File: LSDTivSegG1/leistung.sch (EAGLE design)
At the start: 0 parts

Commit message: developed hard
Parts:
- added C1, C6: 10u, rcl:CPOL-EUE2.5-5
- added C10, C4, C5, C9: 100n, rcl:C-EU025-025X050
- added C2, C3, C7, C8: 1u, rcl:CPOL-EUE2.5-5
- added D1, D2, D7, D8: 1N4001, diode:1N4004
- added D10, D11, D12, D3, D4, D5, D6, D9: 18, diode:ZENER-DIODEZD-10
- added F1, F2, F3: (no value), special:FUSE
- added IC1, IC2, IC3, IC6: IR2184D, irs:IR2184D
- added IC4: 4081N, 40xx:4081N
- added IC5: 4069N, 40xx:4069N
- added Q1, Q2, Q3, Q4, Q5, Q6, Q7, Q8: (no value), transistor-power:PMOSFET_NTO220BV
- added R1, R10, R11, R12, R2, R3, R4, R9: 10, rcl:R-EU_0207/7
- added R13, R14, R15, R16, R5, R6, R7, R8: 47k, rcl:R-EU_0207/7
- added U$1: POWER, lsd2016:POWER
- added X1: 057-010-1, con-panduit:057-010-1
- added X2: MKDSN1,5/2-5,08, con-phoenix-508:MKDSN1,5/2-5,08
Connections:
- new net +15V: C10.1, C4.1, C5.1, C9.1, D1.A, D2.A, D7.A, D8.A, IC1.VCC, IC2.VCC, IC3.VCC, IC6.VCC
- new net +24V: F1.2
- new net +24_HORN: F2.2, F3.2, X2-2.KL
- new net 5V_OUT: X1-1.S
- new net BAT_+: C1.+, C6.+, F1.1, F2.1, F3.1, Q1.D, Q2.D, Q5.D, Q7.D, U$1.BAT_24V_+
- new net BAT_-: C1.-, C10.2, C4.2, C5.2, C6.-, C9.2, IC1.COM, IC2.COM, IC3.COM, IC6.COM, Q3.S, Q4.S, Q6.S, Q8.S, U$1.BAT_24V_-, X2-1.KL
- new net BAT_PWM_OUT: X1-6.S
- new net DIRL_IN: IC1.IN, IC2.IN, IC5A.I, X1-5.S
- new net DIRL_INV: IC3.IN, IC6.IN
- new net DIRL_IN_INV: IC5A.O
- new net DIRR_IN: IC5B.I, X1-7.S
- new net DIRR_IN_INV: IC5B.O
- new net ENABLE: IC4A.I0, IC4B.I0, X1-9.S
- new net GND_OUT: X1-3.S
- new net MOTOR_L_+: C2.-, C7.-, D10.A, D3.A, D4.A, D9.A, IC1.VS, IC2.VS, Q1.S, Q3.D, Q5.S, Q6.D, R15.2, R16.1, R7.2, R8.1, U$1.MOTOR_L_+
- new net MOTOR_L_-: C3.-, C8.-, D11.A, D12.A, D5.A, D6.A, IC3.VS, IC6.VS, Q2.S, Q4.D, Q7.S, Q8.D, R13.1, R14.2, R5.1, R6.2, U$1.MOTOR_L_-
- new net MOTOR_L_ACTIVE: IC1.!SD, IC2.!SD, IC3.!SD, IC4A.O, IC6.!SD
- new net MOTOR_PWM_L: IC4A.I1, X1-2.S
- new net MOTOR_PWM_R: IC4B.I1, X1-4.S
- new net MOTOR_R_+: U$1.MOTOR_R_+
- new net MOTOR_R_-: U$1.MOTOR_R_-
- new net MOTOR_R_ACTIVE: IC4B.O
- new net N$1: IC4P.VDD
- new net N$10: IC2.HO, R1.1
- new net N$11: IC3.HO, R4.2
- new net N$12: IC3.LO, R3.2
- new net N$13: D10.C, Q6.G, R10.2, R15.1
- new net N$14: D9.C, Q5.G, R16.2, R9.2
- new net N$15: IC4C.O
- new net N$16: IC4D.O
- new net N$17: D12.C, Q7.G, R12.1, R13.2
- new net N$18: D11.C, Q8.G, R11.1, R14.1
- new net N$19: IC5C.O
- new net N$2: IC4P.VSS
- new net N$20: IC5C.I
- new net N$21: IC4C.I0
- new net N$22: IC4C.I1
- new net N$23: IC4D.I0
- new net N$24: IC4D.I1
- new net N$25: IC1.LO, R10.1
- new net N$26: IC1.HO, R9.1
- new net N$27: IC6.HO, R12.2
- new net N$28: IC6.LO, R11.2
- new net N$3: IC5P.VDD
- new net N$4: IC5P.VSS
- new net N$5: D4.C, Q3.G, R2.2, R7.1
- new net N$6: D3.C, Q1.G, R1.2, R8.2
- new net N$7: D6.C, Q2.G, R4.1, R5.2
- new net N$8: D5.C, Q4.G, R3.1, R6.1
- new net N$9: IC2.LO, R2.1
- new net NC: X1-8.S
- new net NC2: X1-10.S
- new net VB: C2.+, C3.+, C7.+, C8.+, D1.C, D2.C, D7.C, D8.C, IC1.VB, IC2.VB, IC3.VB, IC6.VB
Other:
- note added: "Control Logic Enable-Signal"
- note added: "Fuses"
- note added: "H-Bridge-1"
- note added: "Mosfets IRFB3077"
- note added: "Mosfets haben Freilaufdiode integriert 210A"
- note added: "Power-Connector"
- note added: "Regelungsboard-Connector"

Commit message: changed naming high/low voltage area
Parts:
- removed C10, C9: 100n, rcl:C-EU025-025X050
- removed C6: 10u, rcl:CPOL-EUE2.5-5
- removed C7, C8: 1u, rcl:CPOL-EUE2.5-5
- removed D10, D11, D12, D9: 18, diode:ZENER-DIODEZD-10
- removed D7, D8: 1N4001, diode:1N4004
- removed IC1, IC6: IR2184D, irs:IR2184D
- removed Q5, Q6, Q7, Q8: (no value), transistor-power:PMOSFET_NTO220BV
- removed R10, R11, R12, R9: 10, rcl:R-EU_0207/7
- removed R13, R14, R15, R16: 47k, rcl:R-EU_0207/7
- added C11: 10u, rcl:CPOL-EUE2.5-5
- added C12, C13: 1u, rcl:CPOL-EUE2.5-5
- added C14, C15: 100n, rcl:C-EU025-025X050
- added D13, D14: 1N4001, diode:1N4004
- added D15, D16, D17, D18: 18, diode:ZENER-DIODEZD-10
- added DC1: TMR, traco_tmr:TMR
- added IC7, IC8: IR2184D, irs:IR2184D
- added Q10, Q11, Q12, Q9: (no value), transistor-power:PMOSFET_NTO220BV
- added R17, R18, R19, R20: 10, rcl:R-EU_0207/7
- added R21, R22, R23, R24: 47k, rcl:R-EU_0207/7
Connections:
- net BAT_PWM_OUT renamed BAT_PWM_OUT_CTL
- removed net 5V_OUT: X1-1.S
- removed net GND_OUT: X1-3.S
- removed net N$13: D10.C, Q6.G, R10.2, R15.1
- removed net N$14: D9.C, Q5.G, R16.2, R9.2
- removed net N$17: D12.C, Q7.G, R12.1, R13.2
- removed net N$18: D11.C, Q8.G, R11.1, R14.1
- removed net N$25: IC1.LO, R10.1
- removed net N$26: IC1.HO, R9.1
- removed net N$27: IC6.HO, R12.2
- removed net N$28: IC6.LO, R11.2
- new net 5V_OUT_CTL: DC1.+VOUT, X1-1.S
- new net DIRL_IN_CTL: X1-5.S
- new net DIRR_INV: IC8.IN
- new net DIRR_IN_CTL: X1-7.S
- new net ENABLE_CTL: X1-9.S
- new net GND_OUT_CTL: DC1.-VOUT, X1-3.S
- new net MOTOR_PWM_L_CTL: X1-2.S
- new net MOTOR_PWM_R_CTL: X1-4.S
- new net N$29: D16.C, Q10.G, R18.2, R23.1
- new net N$30: D15.C, Q9.G, R17.2, R24.2
- new net N$31: D18.C, Q11.G, R20.1, R21.2
- new net N$32: D17.C, Q12.G, R19.1, R22.1
- new net N$33: IC7.LO, R18.1
- new net N$34: IC7.HO, R17.1
- new net N$35: IC8.HO, R20.2
- new net N$36: IC8.LO, R19.2
- net +15V: now also C14.1, C15.1, D13.A, D14.A, IC7.VCC, IC8.VCC; no longer C10.1, C9.1, D7.A, D8.A, IC1.VCC, IC6.VCC
- net +24V: now also DC1.+VIN
- net BAT_+: now also C11.+, Q11.D, Q9.D; no longer C6.+, Q5.D, Q7.D
- net BAT_-: now also C11.-, C14.2, C15.2, DC1.-VIN, IC7.COM, IC8.COM, Q10.S, Q12.S; no longer C10.2, C6.-, C9.2, IC1.COM, IC6.COM, Q6.S, Q8.S
- net DIRL_IN: no longer IC1.IN, X1-5.S
- net DIRL_INV: no longer IC6.IN
- net DIRR_IN: now also IC7.IN; no longer X1-7.S
- net ENABLE: no longer X1-9.S
- net MOTOR_L_+: no longer C7.-, D10.A, D9.A, IC1.VS, Q5.S, Q6.D, R15.2, R16.1
- net MOTOR_L_-: no longer C8.-, D11.A, D12.A, IC6.VS, Q7.S, Q8.D, R13.1, R14.2
- net MOTOR_L_ACTIVE: no longer IC1.!SD, IC6.!SD
- net MOTOR_PWM_L: no longer X1-2.S
- net MOTOR_PWM_R: no longer X1-4.S
- net MOTOR_R_+: now also C12.-, D15.A, D16.A, IC7.VS, Q10.D, Q9.S, R23.2, R24.1
- net MOTOR_R_-: now also C13.-, D17.A, D18.A, IC8.VS, Q11.S, Q12.D, R21.1, R22.2
- net MOTOR_R_ACTIVE: now also IC7.!SD, IC8.!SD
- net VB: now also C12.+, C13.+, D13.C, D14.C, IC7.VB, IC8.VB; no longer C7.+, C8.+, D7.C, D8.C, IC1.VB, IC6.VB
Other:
- note added: "DCDC Converter"
- note added: "H-Bridge-1-Left"
- note added: "H-Bridge-2-Right"
- note added: "On/Off NC for On State"
- note added: "_CTL indicates position on LOW-Voltage Side of board"
- note removed: "H-Bridge-1"

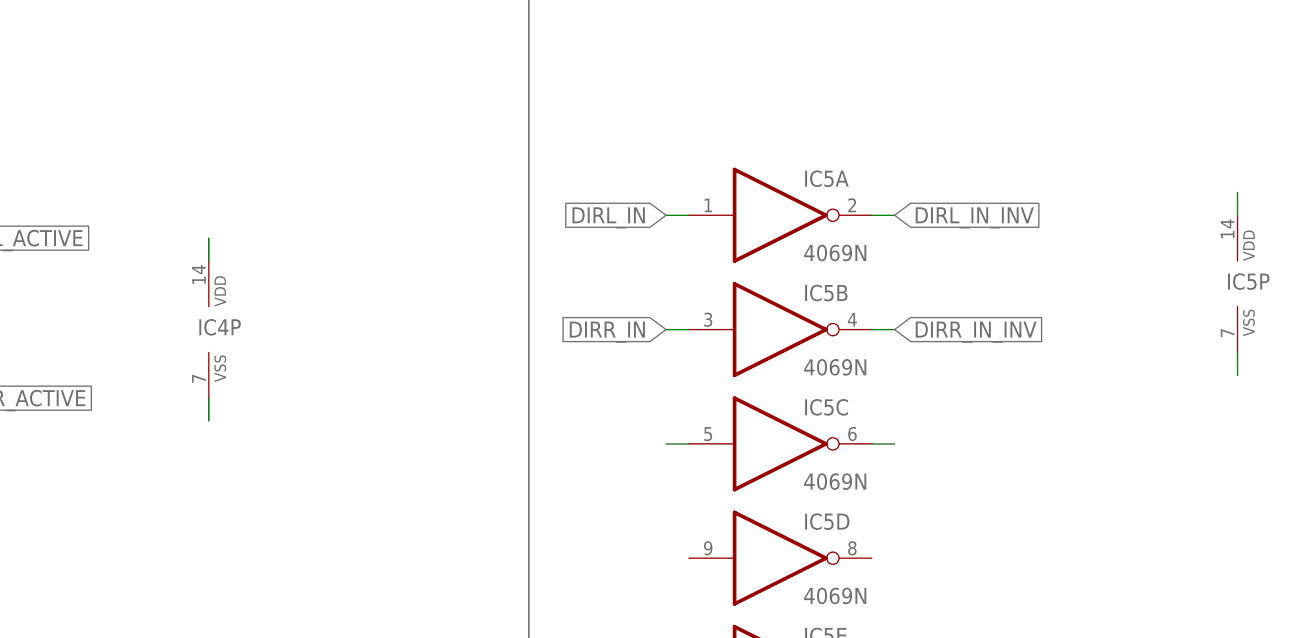
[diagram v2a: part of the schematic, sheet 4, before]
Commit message: added supply to logic gates
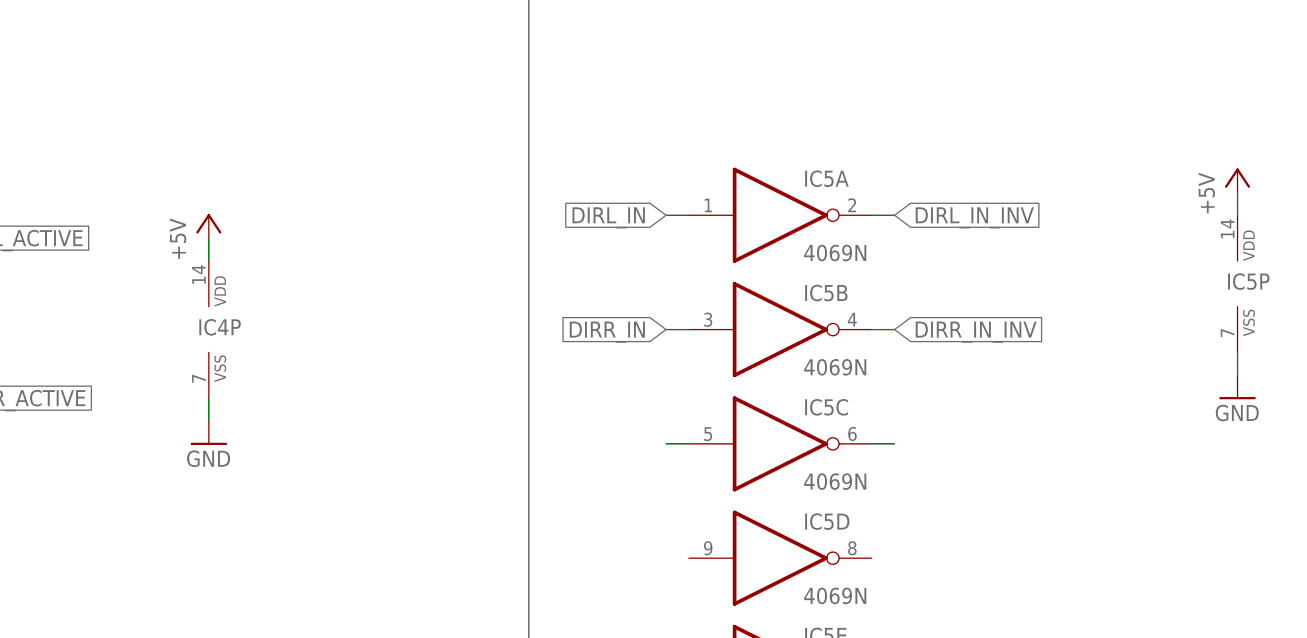
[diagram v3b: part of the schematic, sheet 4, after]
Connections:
- removed net N$1: IC4P.VDD
- removed net N$2: IC4P.VSS
- removed net N$3: IC5P.VDD
- removed net N$4: IC5P.VSS
- new net +5V: IC4P.VDD, IC5P.VDD
- new net GND: IC4P.VSS, IC5P.VSS

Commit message: merged alexs schmeatic with the one from dominik
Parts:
- added C10, C16: 100n, rcl:C-EU025-025X050
- added C6: 1000u, rcl:CPOL-EUE2.5-5V
- added C7: 100u, rcl:CPOL-EUE2.5-5V
- added C8: 100u, rcl:CPOL-EUE2.5-7
- added C9: 1000u, rcl:CPOL-EUE5-13
- added D7: 1N 5711, diode:SCHOTTKY-DIODECB417-15
- added D8: 1N 5711, diode:SCHOTTKY-DIODECB429-15
- added IC1: LM 2576 T5,0, LM2576:LM2576-T05A
- added IC10, IC11: LTV844, lsd2016:LTV844
- added IC6: LM 2576 T15, LM2576:LM2576-T05A
- added IC9: TINY13-20PU, atmel:TINY13-20PU
- added L1, L2: 100u, rcl:L-EU0204/5
- added LED1, LED2: blau, led:LED3MM
- added R10: 16k, rcl:R-EU_0207/10
- added R11, R12, R13, R25, R26, R27: 220, rcl:R-EU_0207/10
- added R14: 100, rcl:R-EU_0207/10
- added R15: 680, rcl:R-EU_0207/10
- added R16: 82k, rcl:R-EU_0207/10
- added R28, R29, R30, R31, R32, R33, R9: 10k, rcl:R-EU_0207/10
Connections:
- new net ADC: IC9.PB4/PCINT4/ADC2, R10.2, R16.1
- new net BAT_PWM_IN: IC9.PB0/PCINT0/AIN0/OC0A/MOSI, R25.1
- new net MOTOR_PWN_L_CTL: R26.1
- new net N$1: D7.C, IC1.+V_OUT, L1.1
- new net N$13: IC10G$1.A, R11.2
- new net N$14: IC10G$2.A, R12.2
- new net N$17: IC10G$3.A, R13.2
- new net N$18: IC10G$4.A, R25.2
- new net N$2: LED1.A, R14.1
- new net N$25: IC11G$2.A, R27.2
- new net N$26: IC11G$1.A, R26.2
- new net N$3: LED2.A, R15.2
- new net N$4: D8.C, IC6.+V_OUT, L2.1
- new net RESET: C16.1, IC9.PB5/PCINT5/!RESET!/ADC0/DW, R9.2
- net +15V: now also C9.+, IC6.FB, L2.2, R15.1
- net +24V: now also C7.+, C8.+, IC1.+V_IN, IC6.+V_IN, R16.2
- net +5V: now also C10.2, C6.+, IC1.FB, IC9.VCC, L1.2, R14.2, R28.1, R29.1, R30.1, R32.1, R33.1, R9.1
- net 5V_OUT_CTL: now also R31.1
- net BAT_PWM_OUT_CTL: now also IC10G$4.COL, R31.2
- net DIRL_IN: now also IC10G$1.COL, R28.2
- net DIRL_IN_CTL: now also R11.1
- net DIRR_IN: now also IC10G$2.COL, R29.2
- net DIRR_IN_CTL: now also R12.1
- net ENABLE: now also IC10G$3.COL, R30.2
- net ENABLE_CTL: now also R13.1
- net GND: now also C10.1, C16.2, C6.-, C7.-, C8.-, C9.-, D7.A, D8.A, IC1.GND, IC1._EN/DIS, IC10G$1.EMIT, IC10G$2.EMIT, IC10G$3.EMIT, IC10G$4.C, IC11G$1.EMIT, IC11G$2.EMIT, IC6.GND, IC6._EN/DIS, IC9.GND, LED1.C, LED2.C, R10.1
- net GND_OUT_CTL: now also IC10G$1.C, IC10G$2.C, IC10G$3.C, IC10G$4.EMIT, IC11G$1.C, IC11G$2.C
- net MOTOR_PWM_L: now also IC11G$1.COL, R32.2
- net MOTOR_PWM_R: now also IC11G$2.COL, R33.2
- net MOTOR_PWM_R_CTL: now also R27.1

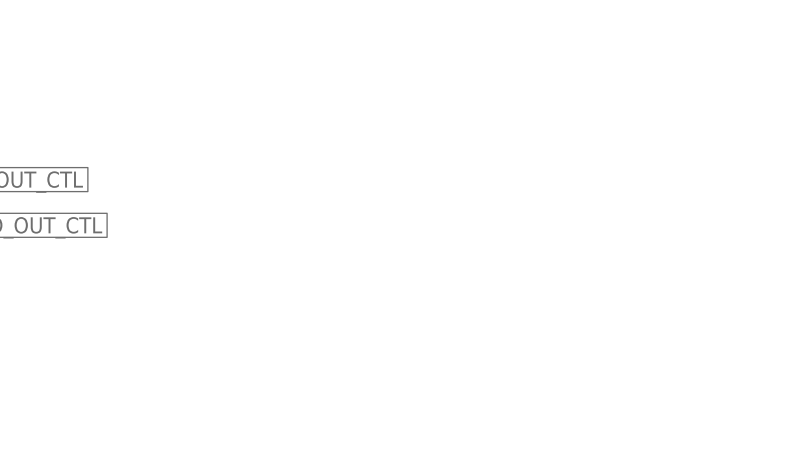
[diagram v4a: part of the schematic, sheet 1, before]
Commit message: added 5V status led to LST side
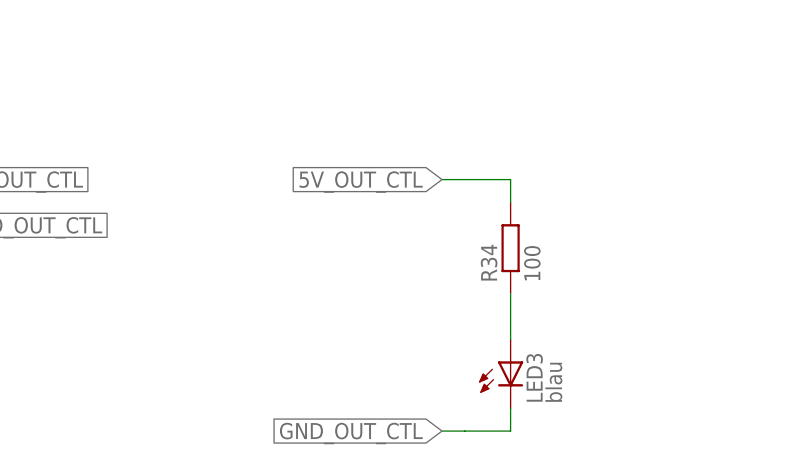
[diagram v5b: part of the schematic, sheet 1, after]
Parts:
- added LED3: blau, led:LED3MM
- added R34: 100, rcl:R-EU_0207/10
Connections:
- new net N$27: LED3.A, R34.1
- net 5V_OUT_CTL: now also R34.2
- net GND_OUT_CTL: now also LED3.C
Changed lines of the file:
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@@
 <part name="GND19" library="supply1" deviceset="GND" device=""/>
 <part name="FRAME8" library="frames" deviceset="FRAME_A_L" device=""/>
+<part name="LED3" library="led" deviceset="LED" device="3MM" value="blau"/>
+<part name="R34" library="rcl" deviceset="R-EU_" device="0207/10" value="100"/>
 </parts>
 <sheets>
@@
 <instance part="X2" gate="-2" x="208.28" y="114.3" rot="R180"/>
 <instance part="DC1" gate="G$1" x="71.12" y="35.56"/>
+<instance part="LED3" gate="G$1" x="152.4" y="17.78"/>
+<instance part="R34" gate="G$1" x="152.4" y="30.48" rot="R90"/>
 </instances>
 <busses>
@@
 <label x="88.9" y="38.1" size="1.778" layer="95" xref="yes"/>
 </segment>
+<segment>
+<pinref part="R34" gate="G$1" pin="2"/>
+<wire x1="152.4" y1="35.56" x2="152.4" y2="38.1" width="0.1524" layer="91"/>
+<wire x1="152.4" y1="38.1" x2="144.78" y2="38.1" width="0.1524" layer="91"/>
+<label x="144.78" y="38.1" size="1.778" layer="95" rot="R180" xref="yes"/>
+</segment>
 </net>
 <net name="GND_OUT_CTL" class="0">
@@
 <label x="88.9" y="33.02" size="1.778" layer="95" xref="yes"/>
 </segment>
+<segment>
+<pinref part="LED3" gate="G$1" pin="C"/>
+<wire x1="152.4" y1="12.7" x2="152.4" y2="10.16" width="0.1524" layer="91"/>
+<wire x1="152.4" y1="10.16" x2="147.32" y2="10.16" width="0.1524" layer="91"/>
+<wire x1="147.32" y1="10.16" x2="144.78" y2="10.16" width="0.1524" layer="91"/>
+<label x="144.78" y="10.16" size="1.778" layer="95" rot="R180" xref="yes"/>
+</segment>
 </net>
 <net name="DIRL_IN_CTL" class="0">
@@
 </segment>
 </net>
+<net name="N$27" class="0">
+<segment>
+<pinref part="LED3" gate="G$1" pin="A"/>
+<wire x1="152.4" y1="25.4" x2="152.4" y2="20.32" width="0.1524" layer="91"/>
+<pinref part="R34" gate="G$1" pin="1"/>
+</segment>
+</net>

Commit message: moved decoupling to regelungsplatine
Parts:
- removed DC1: TMR, traco_tmr:TMR
- removed IC10, IC11: LTV844, lsd2016:LTV844
- removed LED3: blau, led:LED3MM
- removed R11, R12, R13, R25, R26, R27: 220, rcl:R-EU_0207/10
- removed R28, R29, R30, R31, R32, R33: 10k, rcl:R-EU_0207/10
- removed R34: 100, rcl:R-EU_0207/10
- added C17, C18: 100nF, rcl:C-EU025-025X050
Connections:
- removed net 5V_OUT_CTL: DC1.+VOUT, R31.1, R34.2, X1-1.S
- removed net BAT_-: C1.-, C11.-, C14.2, C15.2, C4.2, C5.2, DC1.-VIN, IC2.COM, IC3.COM, IC7.COM, IC8.COM, Q10.S, Q12.S, Q3.S, Q4.S, U$1.BAT_24V_-, X2-1.KL
- removed net BAT_PWM_OUT_CTL: IC10G$4.COL, R31.2, X1-6.S
- removed net DIRL_IN: IC10G$1.COL, IC2.IN, IC5A.I, R28.2
- removed net DIRL_IN_CTL: R11.1, X1-5.S
- removed net DIRR_IN: IC10G$2.COL, IC5B.I, IC7.IN, R29.2
- removed net DIRR_IN_CTL: R12.1, X1-7.S
- removed net ENABLE_CTL: R13.1, X1-9.S
- removed net GND_OUT_CTL: DC1.-VOUT, IC10G$1.C, IC10G$2.C, IC10G$3.C, IC10G$4.EMIT, IC11G$1.C, IC11G$2.C, LED3.C, X1-3.S
- removed net MOTOR_PWM_L_CTL: X1-2.S
- removed net MOTOR_PWM_R_CTL: R27.1, X1-4.S
- removed net MOTOR_PWN_L_CTL: R26.1
- removed net N$13: IC10G$1.A, R11.2
- removed net N$14: IC10G$2.A, R12.2
- removed net N$17: IC10G$3.A, R13.2
- removed net N$18: IC10G$4.A, R25.2
- removed net N$25: IC11G$2.A, R27.2
- removed net N$26: IC11G$1.A, R26.2
- removed net N$27: LED3.A, R34.1
- removed net NC: X1-8.S
- new net BAT_PWM: X1-6.S
- new net DIRL: IC2.IN, IC5A.I, X1-5.S
- new net DIRR: IC5B.I, IC7.IN, X1-7.S
- net +24V: now also X1-1.S; no longer DC1.+VIN
- net +5V: now also C17.1, C18.1, X1-8.S; no longer R28.1, R29.1, R30.1, R32.1, R33.1
- net BAT_PWM_IN: no longer R25.1
- net ENABLE: now also X1-9.S; no longer IC10G$3.COL, R30.2
- net GND: now also C1.-, C11.-, C14.2, C15.2, C17.2, C18.2, C4.2, C5.2, IC2.COM, IC3.COM, IC7.COM, IC8.COM, Q10.S, Q12.S, Q3.S, Q4.S, U$1.BAT_24V_-, X1-3.S, X2-1.KL; no longer IC10G$1.EMIT, IC10G$2.EMIT, IC10G$3.EMIT, IC10G$4.C, IC11G$1.EMIT, IC11G$2.EMIT
- net MOTOR_PWM_L: now also X1-2.S; no longer IC11G$1.COL, R32.2
- net MOTOR_PWM_R: now also X1-4.S; no longer IC11G$2.COL, R33.2
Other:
- note removed: "DCDC Converter"
- note removed: "On/Off NC for On State"

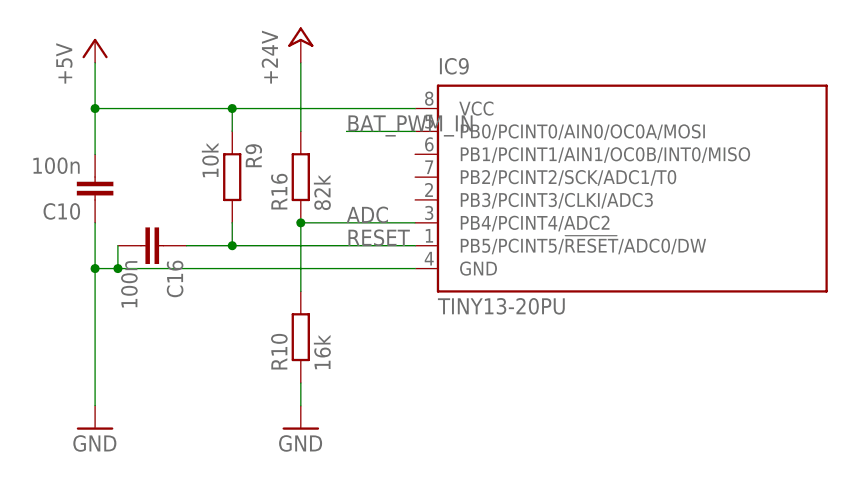
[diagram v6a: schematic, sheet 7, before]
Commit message: replaced resistor with potentiometer in voltage devider for battery monitoring
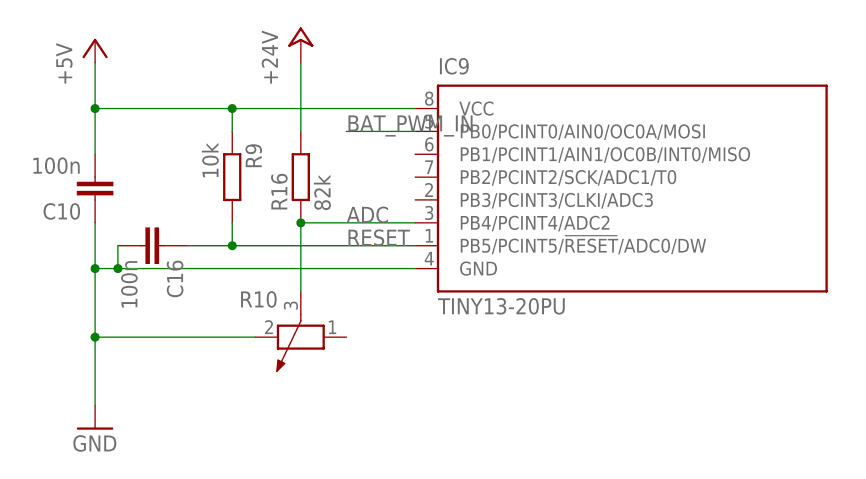
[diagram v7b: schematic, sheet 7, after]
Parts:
- R10: value 16k -> (none); device rcl:R-EU_0207/10 -> rcl:POTENTIOMETER_PT-10
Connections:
- net ADC: now also R10.3; no longer R10.2
- net GND: now also R10.2; no longer R10.1
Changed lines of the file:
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@@
 <part name="P+8" library="supply1" deviceset="+24V" device=""/>
 <part name="R16" library="rcl" deviceset="R-EU_" device="0207/10" value="82k"/>
-<part name="R10" library="rcl" deviceset="R-EU_" device="0207/10" value="16k"/>
-<part name="GND17" library="supply1" deviceset="GND" device=""/>
 <part name="FRAME7" library="frames" deviceset="FRAME_A_L" device=""/>
 <part name="GND20" library="supply1" library_urn="urn:adsk.eagle:library:371" deviceset="GND" device=""/>
@@
 <part name="C17" library="rcl" library_urn="urn:adsk.eagle:library:334" deviceset="C-EU" device="025-025X050" package3d_urn="urn:adsk.eagle:package:23629/2" value="100nF"/>
 <part name="C18" library="rcl" library_urn="urn:adsk.eagle:library:334" deviceset="C-EU" device="025-025X050" package3d_urn="urn:adsk.eagle:package:23629/2" value="100nF"/>
+<part name="R10" library="rcl" library_urn="urn:adsk.eagle:library:334" deviceset="POTENTIOMETER_" device="PT-10" package3d_urn="urn:adsk.eagle:package:23786/1"/>
 </parts>
 <sheets>
@@
 <instance part="P+8" gate="1" x="111.76" y="121.92"/>
 <instance part="R16" gate="G$1" x="111.76" y="106.68" rot="R90"/>
-<instance part="R10" gate="G$1" x="111.76" y="88.9" rot="R90"/>
-<instance part="GND17" gate="1" x="111.76" y="78.74"/>
 <instance part="FRAME7" gate="G$1" x="0" y="0"/>
 <instance part="FRAME7" gate="G$2" x="172.72" y="0"/>
+<instance part="R10" gate="1" x="111.76" y="88.9" rot="R180"/>
 </instances>
 <busses>
@@
 <pinref part="GND13" gate="1" pin="GND"/>
 <wire x1="91.44" y1="96.52" x2="88.9" y2="96.52" width="0.1524" layer="91"/>
-<wire x1="88.9" y1="96.52" x2="88.9" y2="81.28" width="0.1524" layer="91"/>
+<wire x1="88.9" y1="96.52" x2="88.9" y2="88.9" width="0.1524" layer="91"/>
 <pinref part="C10" gate="G$1" pin="1"/>
+<wire x1="88.9" y1="88.9" x2="88.9" y2="81.28" width="0.1524" layer="91"/>
 <wire x1="88.9" y1="96.52" x2="88.9" y2="101.6" width="0.1524" layer="91"/>
 <junction x="88.9" y="96.52"/>
@@
 <wire x1="91.44" y1="99.06" x2="91.44" y2="96.52" width="0.1524" layer="91"/>
 <junction x="91.44" y="96.52"/>
-</segment>
-<segment>
-<pinref part="R10" gate="G$1" pin="1"/>
-<pinref part="GND17" gate="1" pin="GND"/>
-<wire x1="111.76" y1="83.82" x2="111.76" y2="81.28" width="0.1524" layer="91"/>
+<pinref part="R10" gate="1" pin="2"/>
+<wire x1="106.68" y1="88.9" x2="88.9" y2="88.9" width="0.1524" layer="91"/>
+<junction x="88.9" y="88.9"/>
 </segment>
 </net>
@@
 <label x="116.84" y="101.6" size="1.778" layer="95"/>
 <pinref part="R16" gate="G$1" pin="1"/>
-<pinref part="R10" gate="G$1" pin="2"/>
 <wire x1="111.76" y1="101.6" x2="111.76" y2="93.98" width="0.1524" layer="91"/>
 <junction x="111.76" y="101.6"/>
-</segment>
-</net>
+<pinref part="R10" gate="1" pin="3"/>
+</segment>
+</net>
